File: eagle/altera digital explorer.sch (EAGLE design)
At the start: 87 parts, among them IC1 EPM240T100C4, IC2 PIC18F14K50SO, IC3 MCP1703T-3302E/MB, J1 CON_HEADER_1X05-PTH, J8 MICRO-USB-5P-ZX62D-B-5P8-MILL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, Q1 12.00 MHz, SW1 SS-12E10, SW2 SS-12E10, SW3 SS-12E10, SW4 SS-12E10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

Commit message: Updates - make schematic nicer, make PDF
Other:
- note added: "Binary Explorer - Altera"
- moved on the sheet: 7SEG1, 7SEG2, C1, C10, C12, C13, C14, C2, C3, C4, C5, C6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

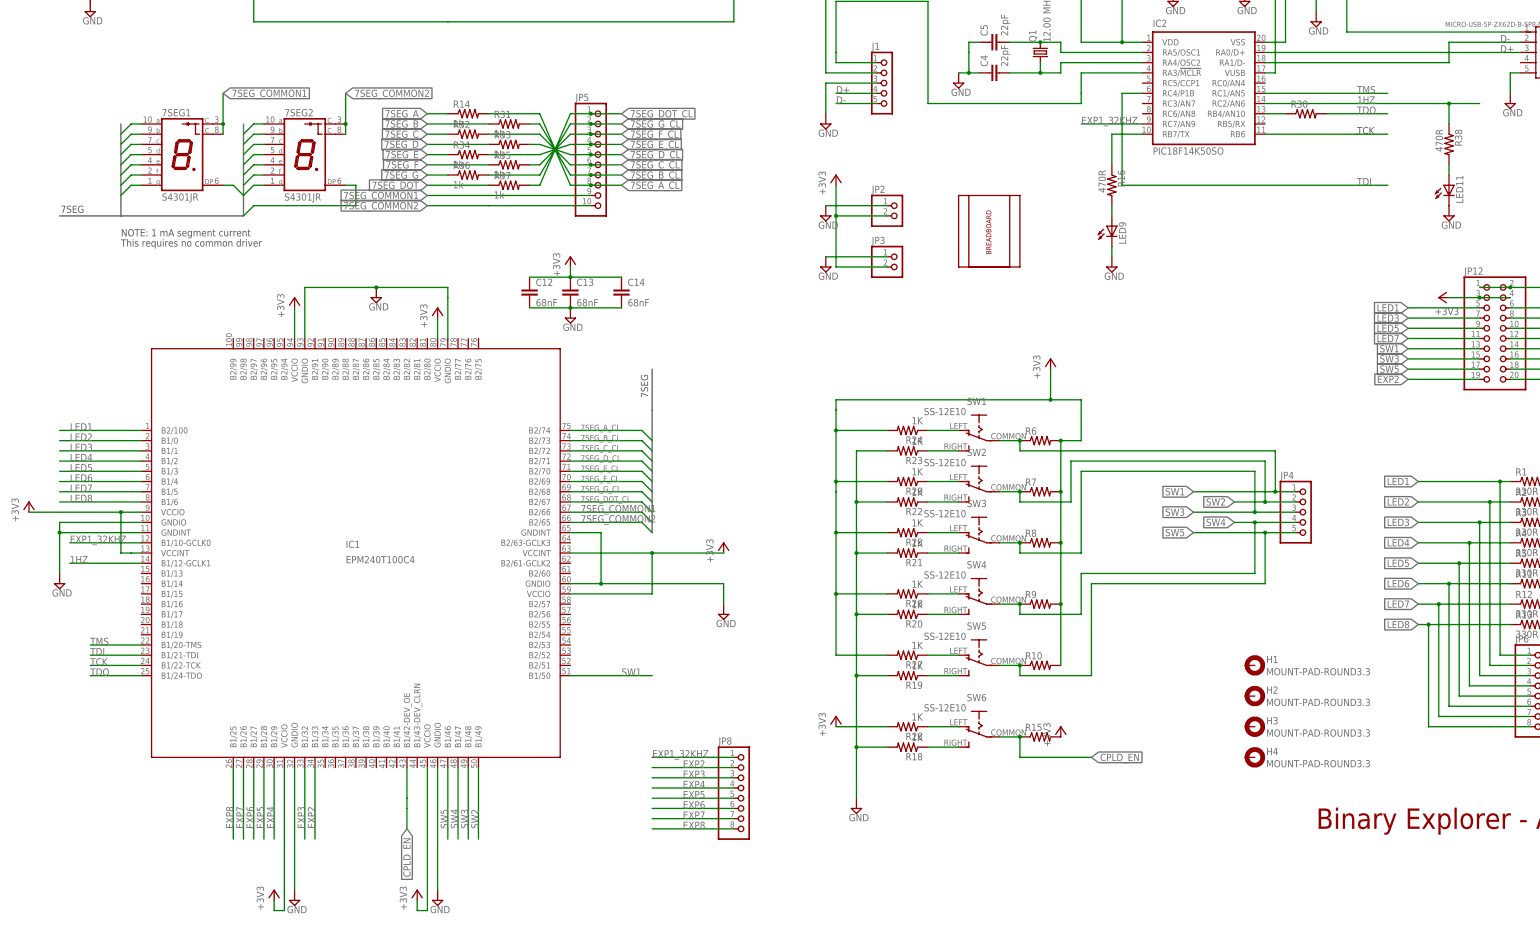
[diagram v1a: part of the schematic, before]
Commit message: PCB update: fix incorrect routing of JTAG programming outputs, change lighthouse to be CPLD controlled, add pushbuttons in addition to switch
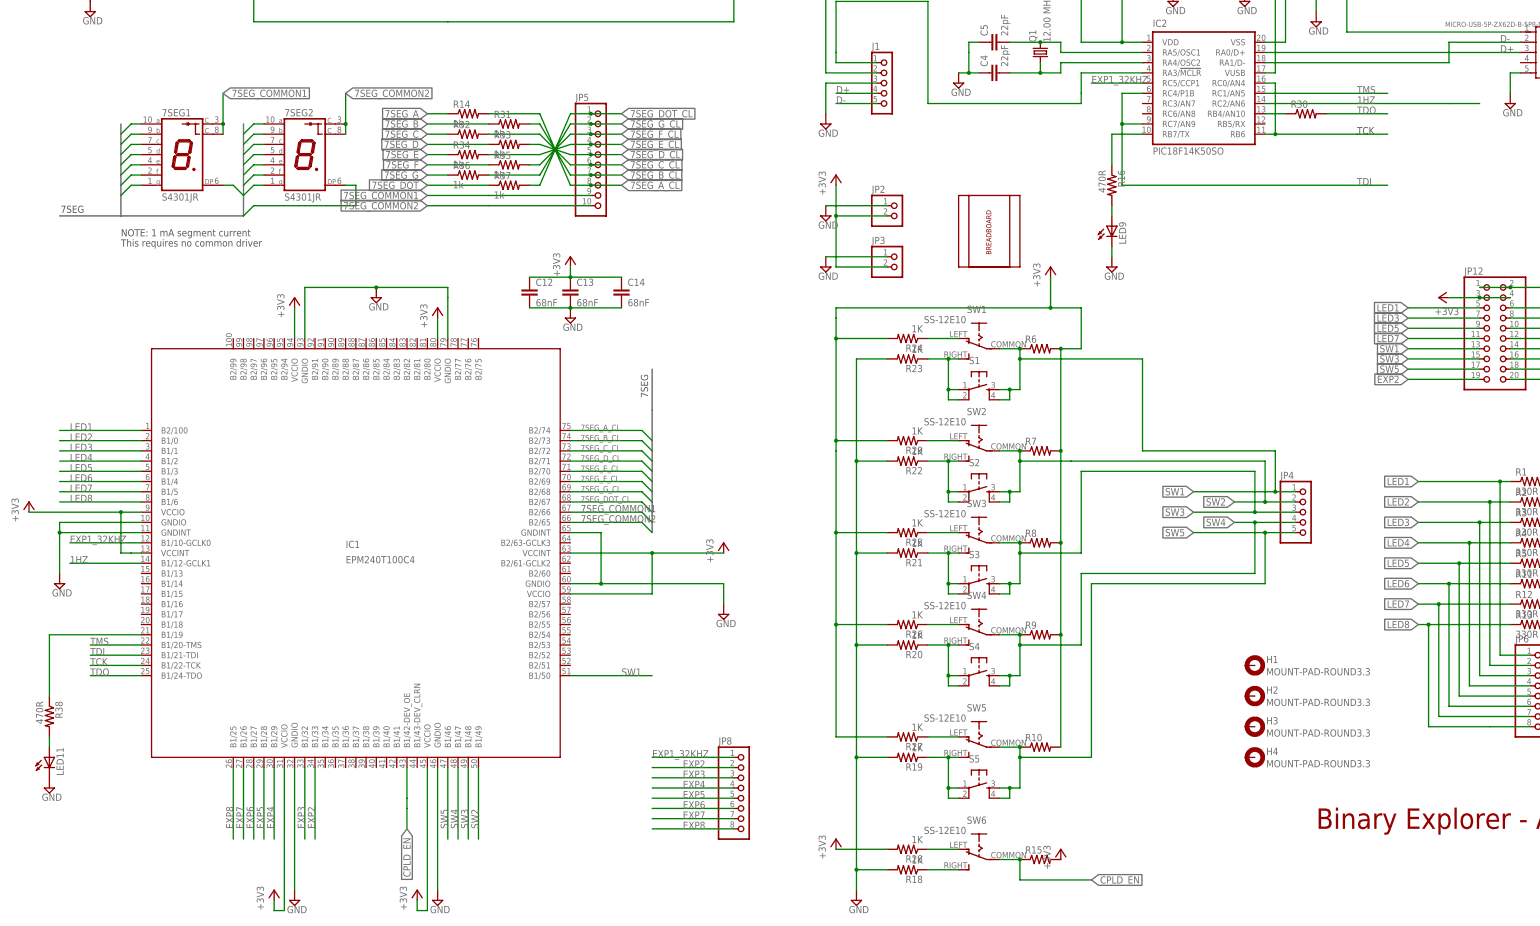
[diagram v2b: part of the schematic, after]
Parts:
- added S1, S2, S3, S4, S5: (no value), SparkFun:TAC_SWITCHPTH
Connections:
- removed net N$20: R20.1, SW4.S
- removed net N$21: R21.1, SW3.S
- removed net N$22: R22.1, SW2.S
- removed net N$33: R23.1, SW1.S
- new net N$15: R20.1, S4.1, S4.2, SW4.S
- new net N$17: R21.1, S3.1, S3.2, SW3.S
- new net N$24: R23.1, S1.1, S1.2, SW1.S
- new net N$4: IC1.B1/19, R38.1
- new net N$5: R22.1, S2.1, S2.2, SW2.S
- net 1HZ: no longer R38.1
- net EXP1_32KHZ: now also IC2.RC5/CCP1; no longer IC2.RC7/AN9
- net N$19: now also S5.1, S5.2
- net SW1: now also S1.3, S1.4
- net SW2: now also S2.3, S2.4
- net SW3: now also S3.3, S3.4
- net SW4: now also S4.3, S4.4
- net SW5: now also S5.3, S5.4
- net TCK: now also IC2.RC0/AN4
- net TDI: now also IC2.RC7/AN9
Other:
- moved on the sheet: LED11, R10, R15, R18, R19, R20, R22, R23, R24, R26, R27, R28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

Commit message: Fix net name for 32khz-->50khz, update schematic print
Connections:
- net EXP1_32KHZ renamed EXP1_50KHZ
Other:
- note added: "04"
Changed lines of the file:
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@@
 <text x="18.034" y="178.562" size="1.778" layer="97">7SEG</text>
 <text x="330.2" y="25.4" size="5.08" layer="94">Binary Explorer - Altera</text>
+<text x="419.1" y="7.62" size="2.54" layer="94">04</text>
 </plain>
 <instances>
@@
 </segment>
 </net>
-<net name="EXP1_32KHZ" class="0">
+<net name="EXP1_50KHZ" class="0">
 <segment>
 <wire x1="167.64" y1="43.18" x2="165.1" y2="43.18" width="0.1524" layer="91"/>

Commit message: Small fixes to schematic
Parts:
- LED1, LED11, LED5: value (none) -> RED
- LED10, LED3, LED4, LED7, LED8, LED9: value (none) -> GRN
- LED2, LED6: value (none) -> YLW
- R10, R15, R6, R7, R8, R9: value (none) -> DNM
- R11: value (none) -> 330R
- R30: value (none) -> 51R
